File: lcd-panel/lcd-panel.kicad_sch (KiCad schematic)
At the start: 50 parts, among them J1 USB wire, J2 LCD FPC connector, J3 Fan Socket, Q1 AO3400A, Q2 AO3401A, Q3 AO3400A, Q4 AO3400A, Q5 2N7002, U1 FT232HL-REEL, U2 93LC56BT-I/OT, U3 USBLC6-2SC6, U4 ATtiny414-SS, Y1 12 MHz, 20 pF load

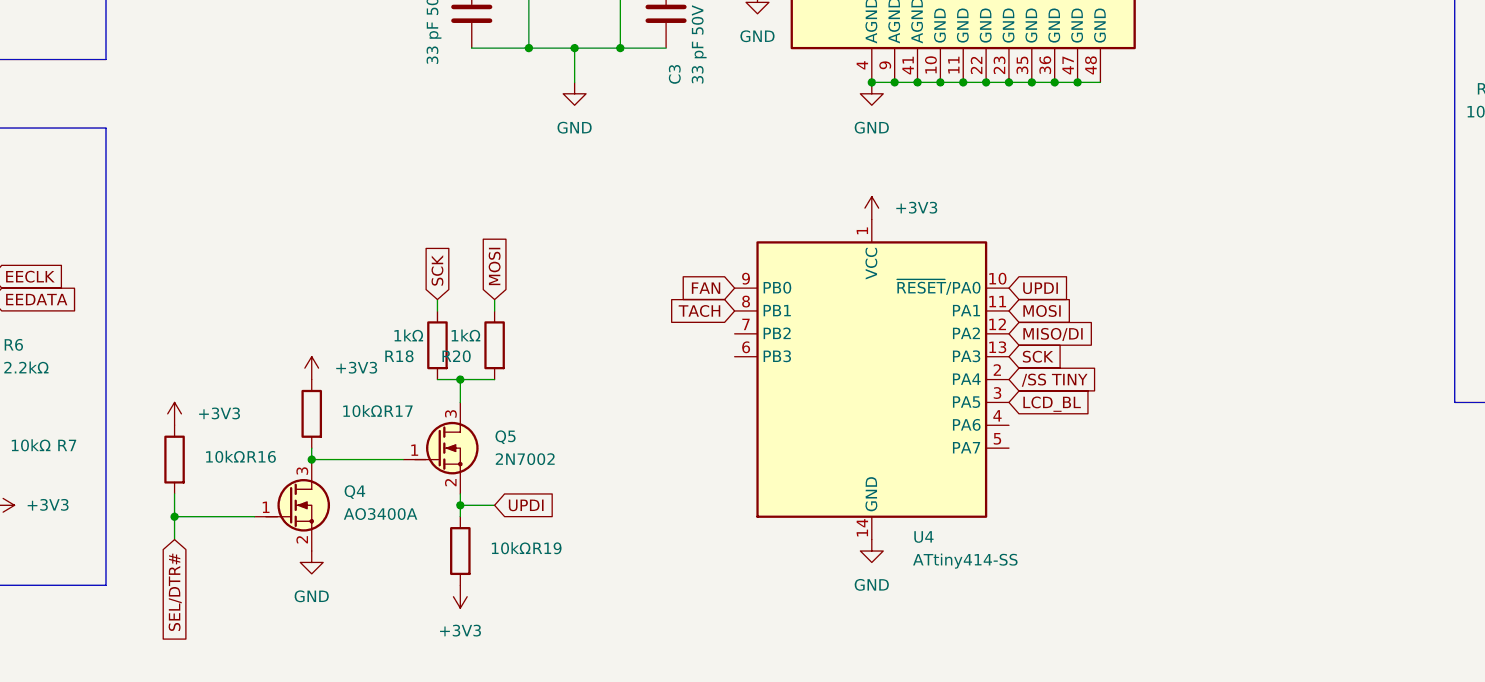
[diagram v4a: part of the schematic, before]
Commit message: Swapping the USB flashing harness for pogo pads
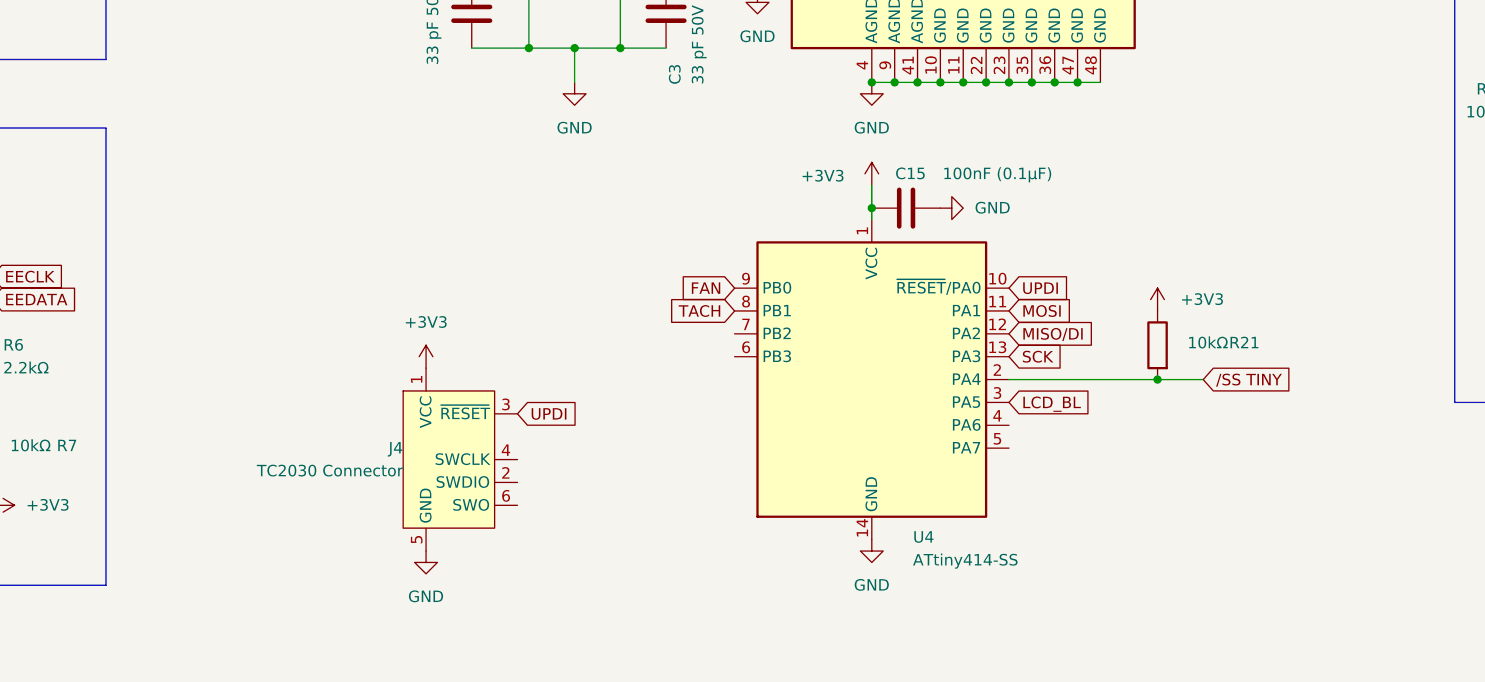
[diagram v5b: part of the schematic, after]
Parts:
- removed Q4: AO3400A, PCM_Package_TO_SOT_SMD_AKL:SOT-23, symbol PCM_Transistor_MOSFET_AKL:AO3400A
- removed Q5: 2N7002, PCM_Package_TO_SOT_SMD_AKL:SOT-23, symbol PCM_Transistor_MOSFET_AKL:2N7002
- removed R16, R17, R19: 10kΩ, Resistor_SMD:R_0402_1005Metric, symbol PCM_Resistor_AKL:R_0603
- removed R18, R20: 1kΩ, Resistor_SMD:R_0402_1005Metric, symbol PCM_Resistor_AKL:R_0603
- added C15: 100nF (0.1µF), Capacitor_SMD:C_0402_1005Metric, symbol PCM_Capacitor_US_AKL:C_Generic
- added J4: TC2030 Connector, Connector:Tag-Connect_TC2030-IDC-NL_2x03_P1.27mm_Vertical, symbol Connector:Conn_ARM_SWD_TagConnect_TC2030-NL
- added R21: 10kΩ, Resistor_SMD:R_0402_1005Metric, symbol PCM_Resistor_AKL:R_0603
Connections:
- net +3V3: now also C15.1, J4.1 (VCC), R21.2
- net GND: now also C15.2, J4.5 (GND)
- net UPDI: now also J4.3 (~{RESET})
- net /SS TINY: now also R21.1

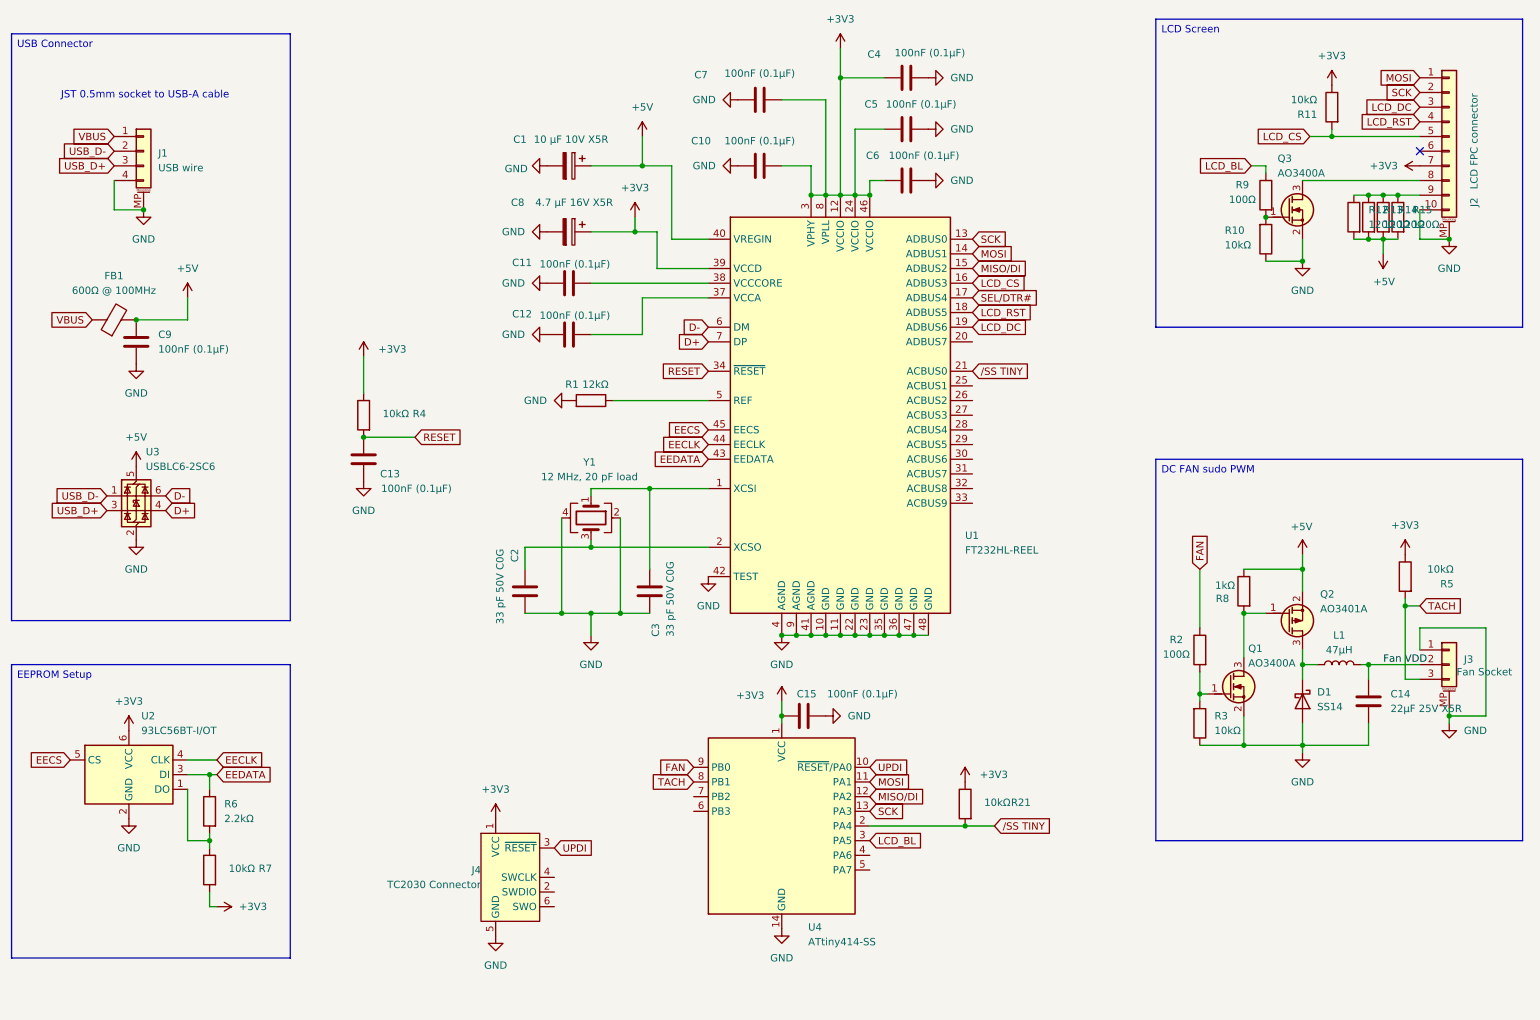
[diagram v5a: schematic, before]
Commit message: Getting most of the components in roughly in the right places
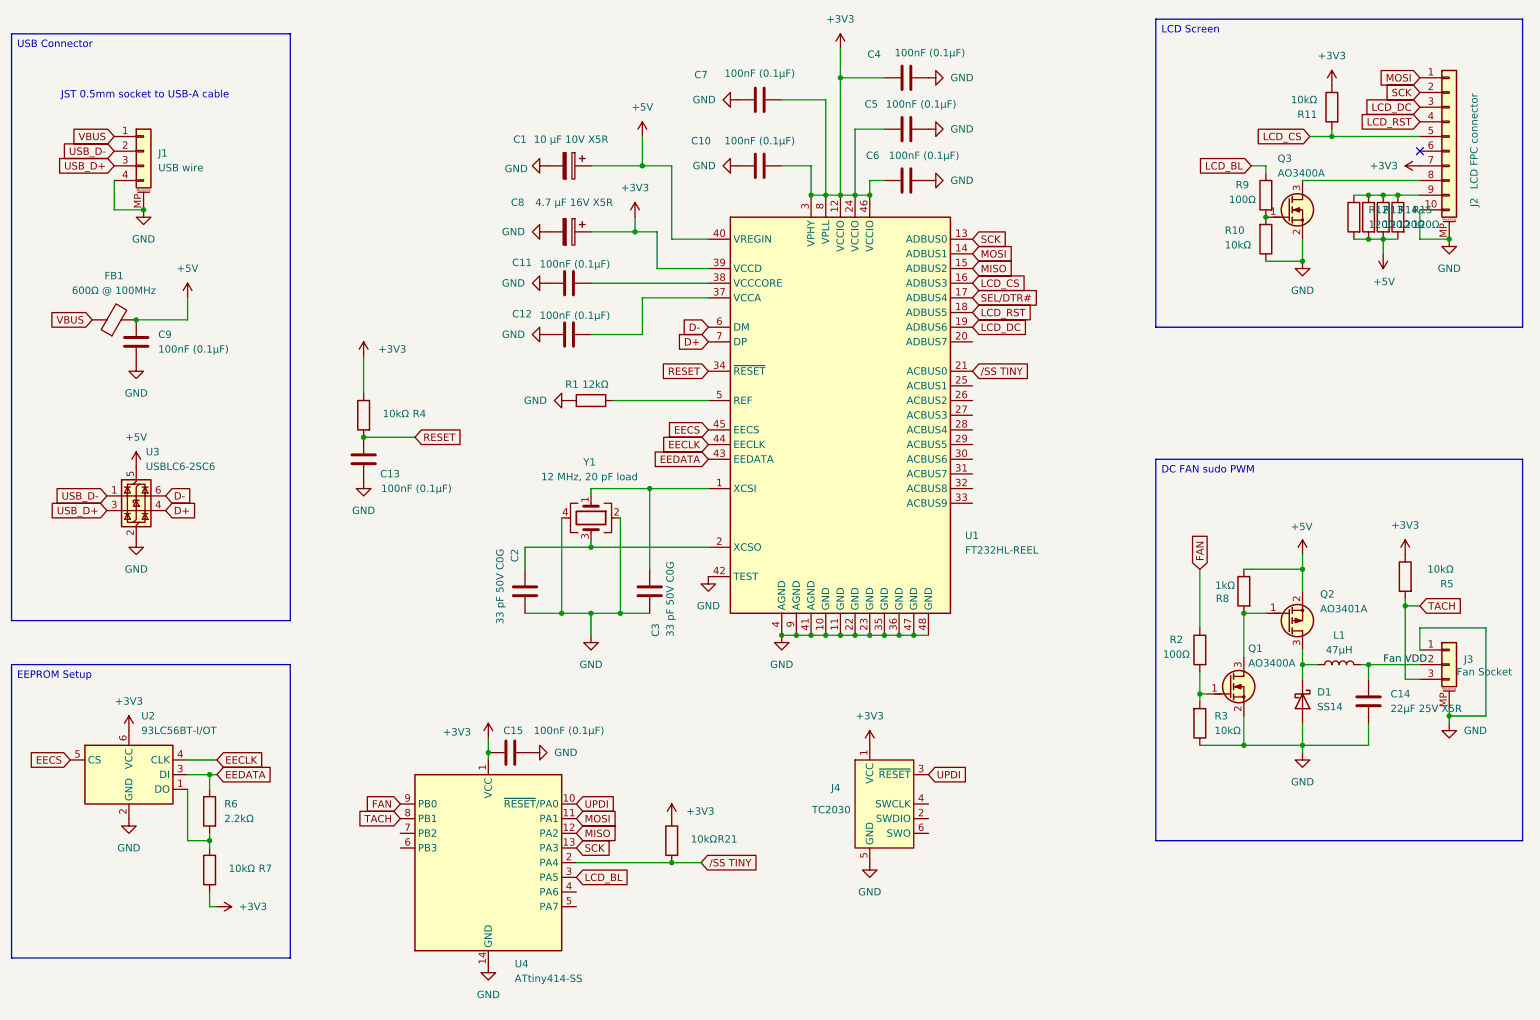
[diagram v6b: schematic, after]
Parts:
- J4: value TC2030 Connector -> TC2030
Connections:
- net MISO/DI renamed MISO
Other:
- moved on the sheet: C15, J4, R21, U4

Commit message: Wiring most of the components together
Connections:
- net SEL/DTR#: no longer names the net of U1.17 (ADBUS4)
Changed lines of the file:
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@@
-		)
-	)
-	(global_label "SEL{slash}DTR#"
-		(shape input)
-		(at 184.15 66.04 0)
-		(fields_autoplaced yes)
-		(effects
-			(font
-				(size 1.27 1.27)
-			)
-			(justify left)
-		)
-		(property "Intersheetrefs" "${INTERSHEET_REFS}"
-			(at 196.6299 66.04 0)
-			(effects
-				(font
-					(size 1.27 1.27)
-				)
-				(justify left)
-				(hide yes)
-			)
 		)
 	)
